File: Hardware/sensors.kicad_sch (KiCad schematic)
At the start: 26 parts, among them IC1 BMP388, IC2 ICM-42688-P, J1 Conn_Coaxial, J12 Conn_Coaxial, U2 MAX-M10S, U3 74LVC1GU04

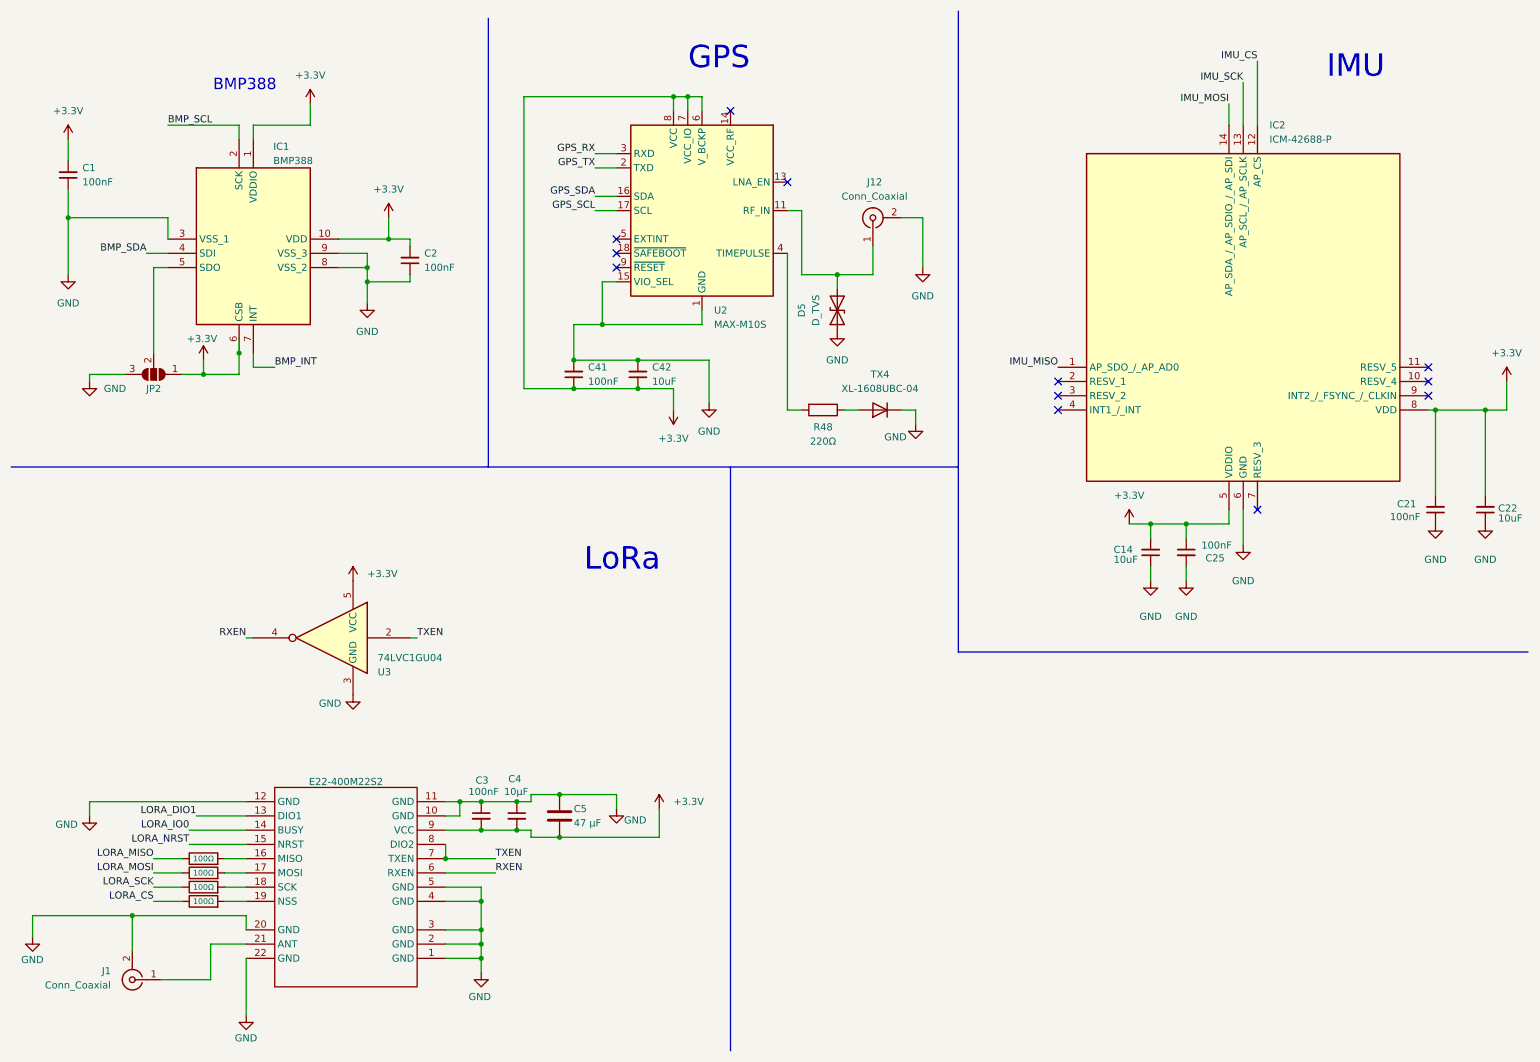
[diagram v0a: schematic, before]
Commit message: pieliku IMU un vēl kaut ko
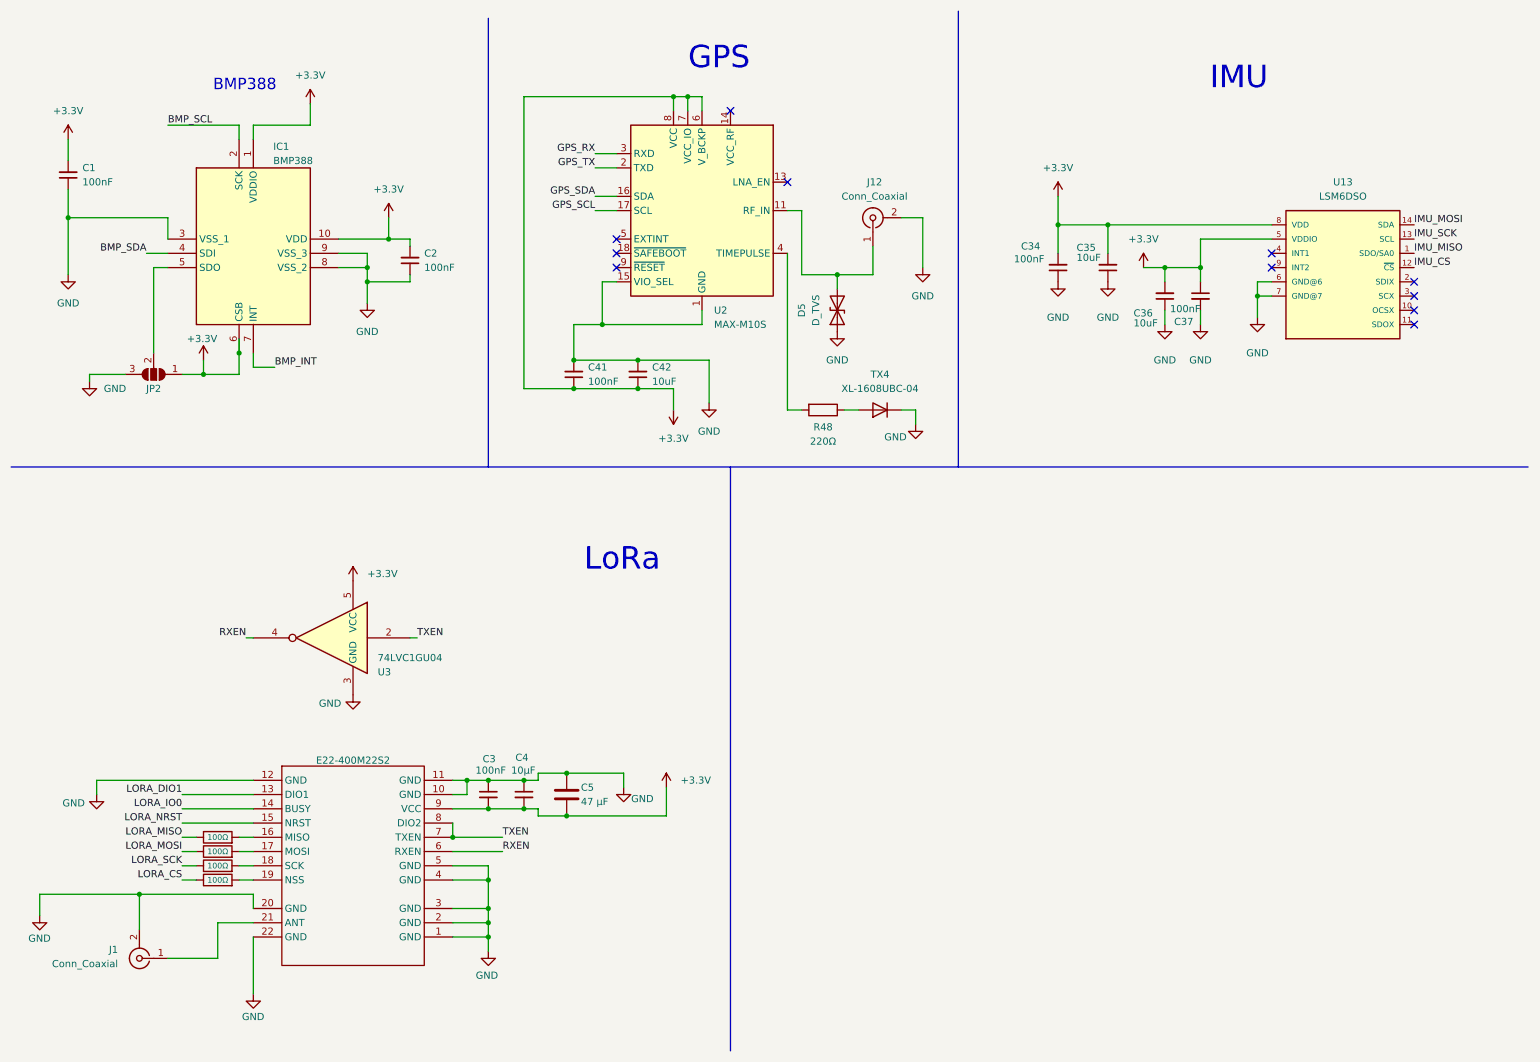
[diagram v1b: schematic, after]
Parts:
- removed C14, C22: 10uF, Capacitor_SMD:C_0402_1005Metric, symbol Device:C_Small
- removed C21, C25: 100nF, Capacitor_SMD:C_0402_1005Metric, symbol Device:C_Small
- removed IC2: ICM-42688-P, ICM-42688-P:IIM42352, symbol ICM-42688-P:ICM-42688-P
- added C34, C37: 100nF, Capacitor_SMD:C_0402_1005Metric, symbol Device:C_Small
- added C35, C36: 10uF, Capacitor_SMD:C_0402_1005Metric, symbol Device:C_Small
- added U13: LSM6DSO, LSM6DSO:LGA14L, symbol LSM6DSO:LSM6DSO
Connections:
- net +3.3V: now also C34.2, C35.2, C36.2, C37.1, U13.5 (VDDIO), U13.8 (VDD)
- net GND: now also C34.1, C35.1, C36.1, C37.2, U13.6 (GND@6), U13.7 (GND@7)
- net IMU_CS: now also U13.12 (~{CS})
- net IMU_MISO: now also U13.1 (SDO/SA0)
- net IMU_MOSI: now also U13.14 (SDA)
- net IMU_SCK: now also U13.13 (SCL)
- no-connect marks 12 -> 11
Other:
- moved on the sheet: C3, C4, C5, E22-400M22S2, J1
